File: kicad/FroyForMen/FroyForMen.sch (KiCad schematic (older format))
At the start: 22 parts, among them IC1 ESP-WROOM-02U__4MB_, J1 Screw_Terminal_01x02, J2 Conn_01x06, Q1 Q_NPN_BEC, Q2 Q_NPN_BEC, Q3 Q_NPN_BEC, Q4 Q_NPN_BEC, SW1 SW_SPST, U1 BME280

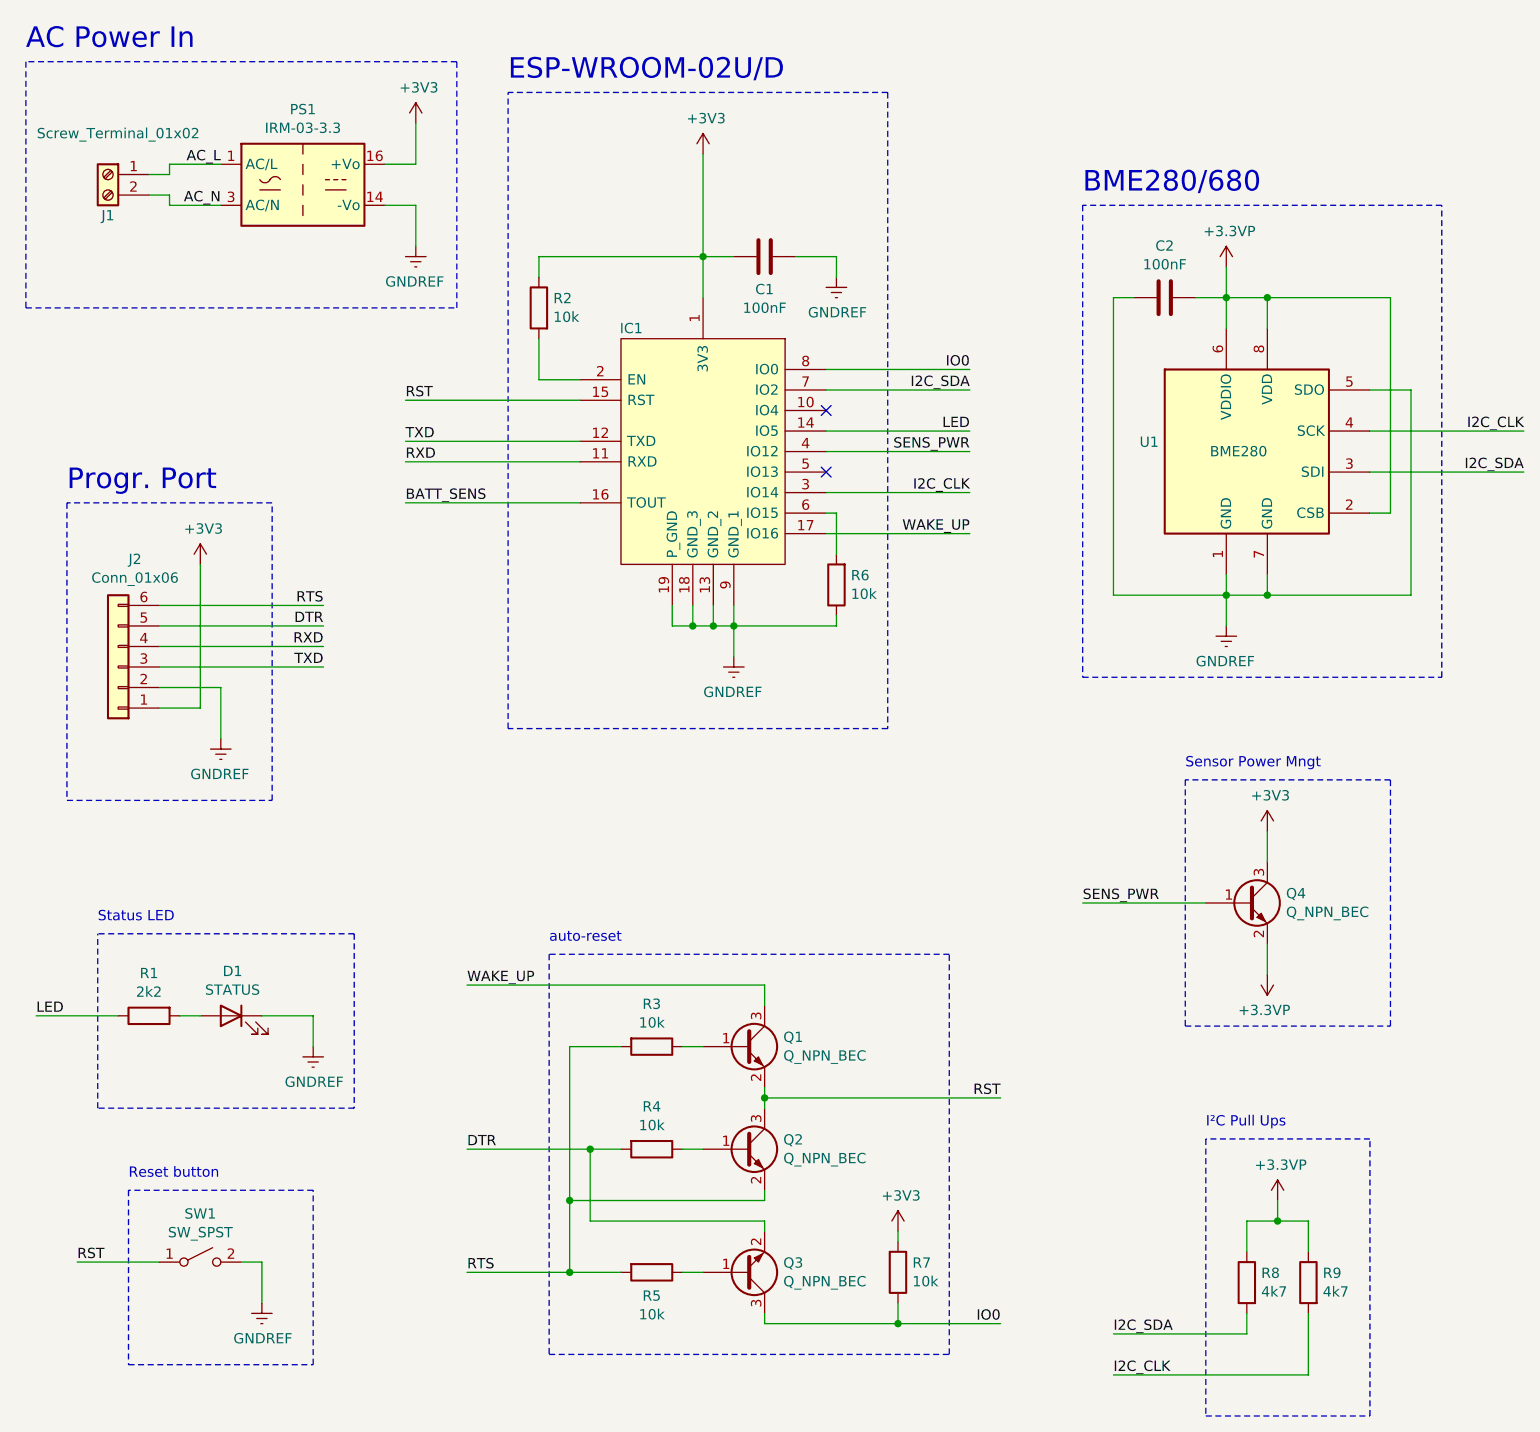
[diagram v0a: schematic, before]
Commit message: FroyForMen v1.3 - removed power transistor, use Omron button
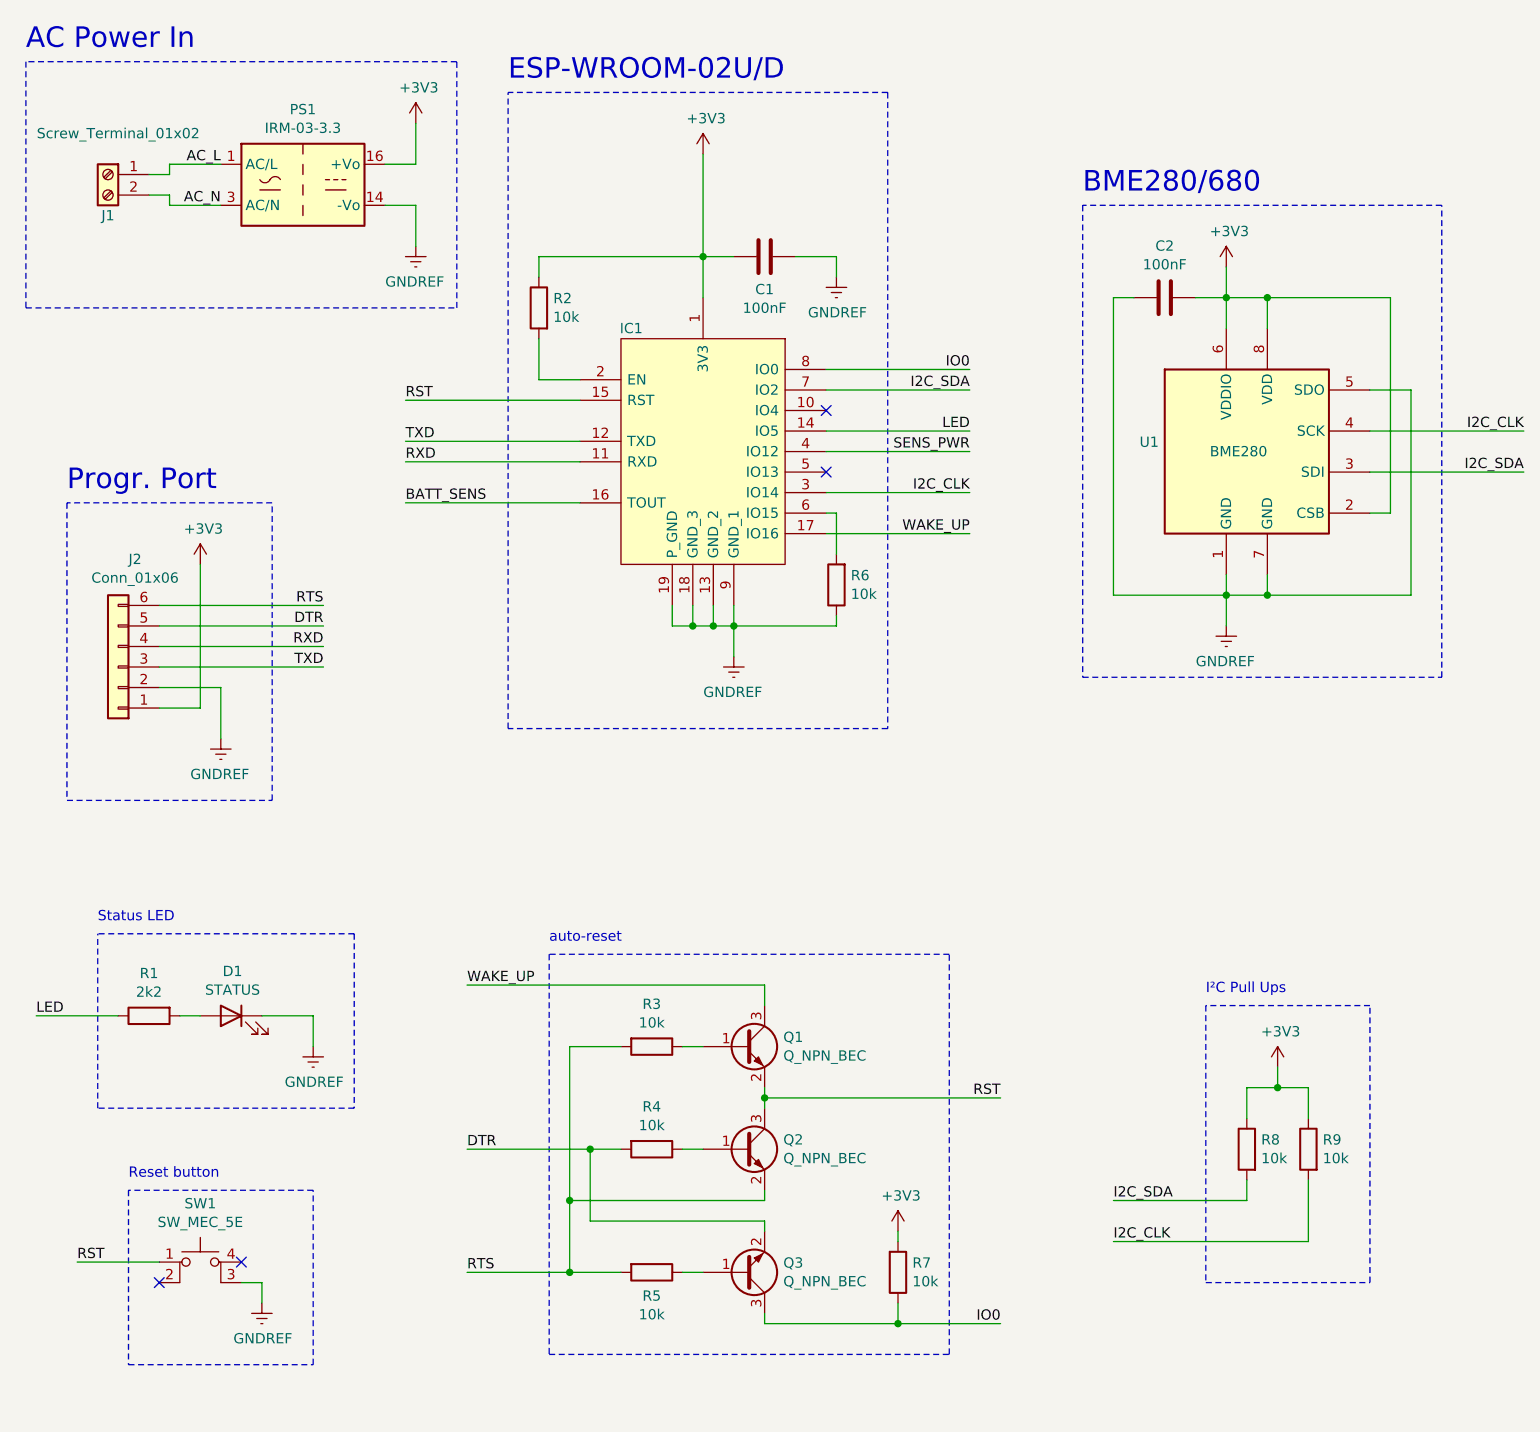
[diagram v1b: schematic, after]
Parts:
- removed Q4: Q_NPN_BEC, Package_TO_SOT_SMD:SOT-23, symbol Device:Q_NPN_BEC
- removed SW1: SW_SPST, Button_Switch_SMD:SW_SPST_CK_RS282G05A3, symbol Switch:SW_SPST
- added SW1: SW_MEC_5E, xrstf:SW_SPST_Omron_B3FS-100xP, symbol Switch:SW_MEC_5E
- D1: footprint LED_SMD:LED_1206_3216Metric_Pad1.42x1.75mm_HandSolder -> LED_SMD:LED_0805_2012Metric
- R8, R9: value 4k7 -> 10k
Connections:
- net +3.3VP is gone; now on net +3V3: C2.2, R8.1, R9.1, U1.2 (CSB), U1.6 (VDDIO), U1.8 (VDD)
- net GNDREF: now also SW1.3 (K)
- net RST: now also SW1.1
- no-connect marks 2 -> 4
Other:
- note removed: "Sensor Power Mngt"
- moved on the sheet: R8, R9
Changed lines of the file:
@@
 F 0 "D1" H 1693 6017 50  0000 C CNN
 F 1 "STATUS" H 1693 5926 50  0000 C CNN
-F 2 "LED_SMD:LED_1206_3216Metric_Pad1.42x1.75mm_HandSolder" H 1700 5800 50  0001 C CNN
+F 2 "LED_SMD:LED_0805_2012Metric" H 1700 5800 50  0001 C CNN
 F 3 "~" H 1700 5800 50  0001 C CNN
 	1    1700 5800
@@
 Wire Wire Line
 	2100 5800 2100 5950
-$Comp
-L Switch:SW_SPST SW1
-U 1 1 60A341F2
-P 1550 7000
-F 0 "SW1" H 1550 7235 50  0000 C CNN
-F 1 "SW_SPST" H 1550 7144 50  0000 C CNN
-F 2 "Button_Switch_SMD:SW_SPST_CK_RS282G05A3" H 1550 7000 50  0001 C CNN
-F 3 "~" H 1550 7000 50  0001 C CNN
-	1    1550 7000
-	1    0    0    -1
-$EndComp
 Wire Wire Line
 	1350 7000 950  7000
@@
 	1    0    0    -1
 $EndComp
-Wire Wire Line
-	1750 7000 1850 7000
-Wire Wire Line
-	1850 7000 1850 7200
 Wire Notes Line
 	1200 7500 2100 7500
@@
 Wire Wire Line
 	7350 2300 7350 3350
-Text Label 6000 7550 0    50   ~ 0
+Text Label 6000 6900 0    50   ~ 0
 I2C_CLK
-Text Label 6000 7350 0    50   ~ 0
+Text Label 6000 6700 0    50   ~ 0
 I2C_SDA
 $Comp
 L Device:R R8
 U 1 1 60D6AC5D
-P 6650 7100
-F 0 "R8" H 6580 7146 50  0000 R CNN
-F 1 "4k7" H 6580 7055 50  0000 R CNN
-F 2 "Resistor_SMD:R_0805_2012Metric" V 6580 7100 50  0001 C CNN
-F 3 "~" H 6650 7100 50  0001 C CNN
-	1    6650 7100
-	-1   0    0    -1
-$EndComp
-Wire Wire Line
-	6650 7350 6000 7350
-Wire Wire Line
-	6650 7250 6650 7350
+P 6650 6450
+F 0 "R8" H 6580 6496 50  0000 R CNN
+F 1 "10k" H 6580 6405 50  0000 R CNN
+F 2 "Resistor_SMD:R_0805_2012Metric" V 6580 6450 50  0001 C CNN
+F 3 "~" H 6650 6450 50  0001 C CNN
+	1    6650 6450
+	-1   0    0    -1
+$EndComp
+Wire Wire Line
+	6650 6700 6000 6700
+Wire Wire Line
+	6650 6600 6650 6700
 $Comp
 L Device:R R9
 U 1 1 60D714B3
-P 6950 7100
-F 0 "R9" H 6880 7146 50  0000 R CNN
-F 1 "4k7" H 6880 7055 50  0000 R CNN
-F 2 "Resistor_SMD:R_0805_2012Metric" V 6880 7100 50  0001 C CNN
-F 3 "~" H 6950 7100 50  0001 C CNN
-	1    6950 7100
-	-1   0    0    -1
-$EndComp
-Wire Wire Line
-	6950 7250 6950 7550
-Wire Wire Line
-	6000 7550 6950 7550
-Wire Wire Line
-	6800 6800 6650 6800
-Wire Wire Line
-	6650 6800 6650 6950
-Wire Wire Line
-	6800 6800 6950 6800
-Wire Wire Line
-	6950 6800 6950 6950
-Connection ~ 6800 6800
-Wire Wire Line
-	6800 6700 6800 6800
-Wire Notes Line
-	6450 7750 7250 7750
-Wire Notes Line
-	7250 7750 7250 6400
-Wire Notes Line
-	7250 6400 6450 6400
-Wire Notes Line
-	6450 6400 6450 7750
-Text Notes 6450 6350 0    50   ~ 0
+P 6950 6450
+F 0 "R9" H 6880 6496 50  0000 R CNN
+F 1 "10k" H 6880 6405 50  0000 R CNN
+F 2 "Resistor_SMD:R_0805_2012Metric" V 6880 6450 50  0001 C CNN
+F 3 "~" H 6950 6450 50  0001 C CNN
+	1    6950 6450
+	-1   0    0    -1
+$EndComp
+Wire Wire Line
+	6950 6600 6950 6900
+Wire Wire Line
+	6000 6900 6950 6900
+Wire Wire Line
+	6800 6150 6650 6150
+Wire Wire Line
+	6650 6150 6650 6300
+Wire Wire Line
+	6800 6150 6950 6150
+Wire Wire Line
+	6950 6150 6950 6300
+Connection ~ 6800 6150
+Wire Wire Line
+	6800 6050 6800 6150
+Wire Notes Line
+	6450 7100 7250 7100
+Wire Notes Line
+	7250 7100 7250 5750
+Wire Notes Line
+	7250 5750 6450 5750
+Wire Notes Line
+	6450 5750 6450 7100
+Text Notes 6450 5700 0    50   ~ 0
 I²C Pull Ups
 $Comp
@@
 	1    0    0    -1
 $EndComp
-$Comp
-L Device:Q_NPN_BEC Q4
-U 1 1 611A415E
-P 6650 5250
-F 0 "Q4" H 6841 5296 50  0000 L CNN
-F 1 "Q_NPN_BEC" H 6841 5205 50  0000 L CNN
-F 2 "Package_TO_SOT_SMD:SOT-23" H 6850 5350 50  0001 C CNN
-F 3 "~" H 6650 5250 50  0001 C CNN
-	1    6650 5250
-	1    0    0    -1
-$EndComp
 Text Label 5300 3050 2    50   ~ 0
 SENS_PWR
 Wire Wire Line
 	5300 3050 4600 3050
-Text Label 5850 5250 0    50   ~ 0
-SENS_PWR
-Wire Wire Line
-	5850 5250 6450 5250
-$Comp
-L power:+3V3 #PWR014
-U 1 1 611AD9EB
-P 6750 4900
-F 0 "#PWR014" H 6750 4750 50  0001 C CNN
-F 1 "+3V3" H 6765 5073 50  0000 C CNN
-F 2 "" H 6750 4900 50  0001 C CNN
-F 3 "" H 6750 4900 50  0001 C CNN
-	1    6750 4900
-	1    0    0    -1
-$EndComp
-Wire Wire Line
-	6750 5050 6750 4900
-$Comp
-L power:+3.3VP #PWR015
-U 1 1 611B333D
-P 6750 5600
-F 0 "#PWR015" H 6900 5550 50  0001 C CNN
-F 1 "+3.3VP" H 6765 5773 50  0000 C CNN
-F 2 "" H 6750 5600 50  0001 C CNN
-F 3 "" H 6750 5600 50  0001 C CNN
-	1    6750 5600
-	-1   0    0    1
-$EndComp
-Wire Wire Line
-	6750 5450 6750 5600
-Wire Notes Line
-	7350 5850 7350 4650
-Wire Notes Line
-	7350 4650 6350 4650
-Wire Notes Line
-	6350 4650 6350 5850
-Wire Notes Line
-	6350 5850 7350 5850
-Text Notes 6350 4600 0    50   ~ 0
-Sensor Power Mngt
-$Comp
-L power:+3.3VP #PWR011
-U 1 1 611D535E
+$Comp
+L power:+3V3 #PWR0101
+U 1 1 615C4B58
 P 6550 2150
-F 0 "#PWR011" H 6700 2100 50  0001 C CNN
-F 1 "+3.3VP" H 6565 2323 50  0000 C CNN
+F 0 "#PWR0101" H 6550 2000 50  0001 C CNN
+F 1 "+3V3" H 6565 2323 50  0000 C CNN
 F 2 "" H 6550 2150 50  0001 C CNN
 F 3 "" H 6550 2150 50  0001 C CNN
@@
 $EndComp
 $Comp
-L power:+3.3VP #PWR?
-U 1 1 611D9307
-P 6800 6700
-F 0 "#PWR?" H 6950 6650 50  0001 C CNN
-F 1 "+3.3VP" H 6815 6873 50  0000 C CNN
-F 2 "" H 6800 6700 50  0001 C CNN
-F 3 "" H 6800 6700 50  0001 C CNN
-	1    6800 6700
-	1    0    0    -1
-$EndComp
+L power:+3V3 #PWR0102
+U 1 1 615C70B2
+P 6800 6050
+F 0 "#PWR0102" H 6800 5900 50  0001 C CNN
+F 1 "+3V3" H 6815 6223 50  0000 C CNN
+F 2 "" H 6800 6050 50  0001 C CNN
+F 3 "" H 6800 6050 50  0001 C CNN
+	1    6800 6050
+	1    0    0    -1
+$EndComp
+$Comp
+L Switch:SW_MEC_5E SW1
+U 1 1 61600B47
+P 1550 7100
+F 0 "SW1" H 1550 7485 50  0000 C CNN
+F 1 "SW_MEC_5E" H 1550 7394 50  0000 C CNN
+F 2 "xrstf:SW_SPST_Omron_B3FS-100xP" H 1550 7400 50  0001 C CNN
+F 3 "http://www.apem.com/int/index.php?controller=attachment&id_attachment=1371" H 1550 7400 50  0001 C CNN
+	1    1550 7100
+	1    0    0    -1
+$EndComp
+Wire Wire Line
+	1750 7100 1850 7100
+Wire Wire Line
+	1850 7100 1850 7200
+NoConn ~ 1750 7000
+NoConn ~ 1350 7100
 $EndSCHEMATC
